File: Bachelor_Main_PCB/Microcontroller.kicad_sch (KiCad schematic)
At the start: 14 parts, among them J3 M20-9990245, J4 M20-9990245, J5 M20-9990245, U3 STM32H7A3ZITxQ, U4 USB3320C-EZK-TR, Y1 SG-210STF 24Mhz

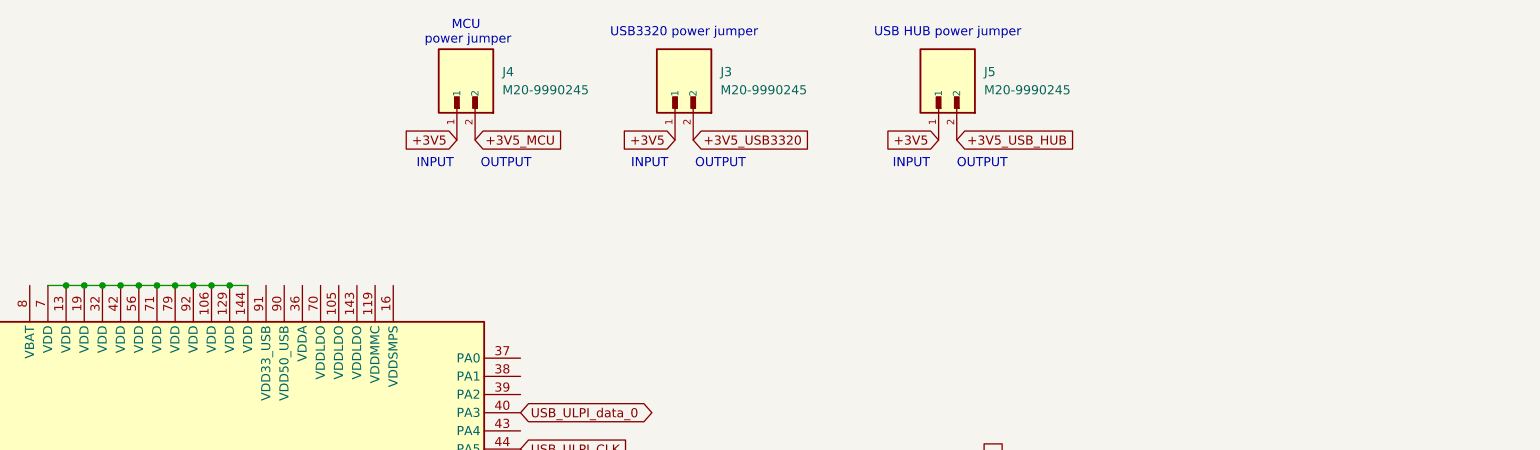
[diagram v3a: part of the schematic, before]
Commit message: Add 2,2uF inductor to MCU
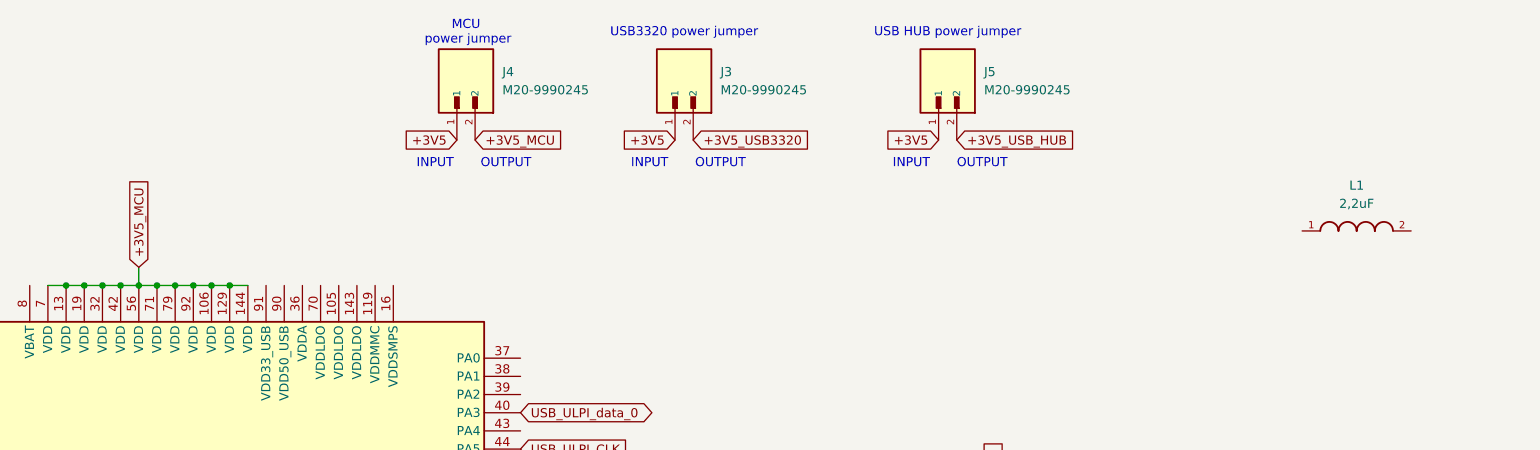
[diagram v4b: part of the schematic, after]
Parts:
- added L1: 2,2uF, DFE252012P-2R2M=P2:INDC2520X120N, symbol DFE252012P-2R2M_P2:DFE252012P-2R2M=P2
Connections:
- net +3V5_MCU: now also U3.106 (VDD), U3.129 (VDD), U3.13 (VDD), U3.144 (VDD), U3.19 (VDD), U3.32 (VDD), U3.42 (VDD), U3.56 (VDD), U3.7 (VDD), U3.71 (VDD), U3.79 (VDD), U3.92 (VDD)
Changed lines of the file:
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@@
 	(wire
 		(pts
+			(xy 90.17 53.34) (xy 90.17 55.88)
+		)
+		(stroke
+			(width 0)
+			(type default)
+		)
+	)
+	(wire
+		(pts
 			(xy 102.87 55.88) (xy 105.41 55.88)
 		)
@@
 		)
 	)
+	(global_label "+3V5_MCU"
+		(shape input)
+		(at 90.17 53.34 90)
+		(fields_autoplaced yes)
+		(effects
+			(font
+				(size 1.27 1.27)
+			)
+			(justify left)
+		)
+		(property "Intersheetrefs" "${INTERSHEET_REFS}"
+			(at 90.17 40.2553 90)
+			(effects
+				(font
+					(size 1.27 1.27)
+				)
+				(justify left)
+				(hide yes)
+			)
+		)
+	)
 	(global_label "USB_ULPI_data_1"
 		(shape bidirectional)
@@
 					(unit 1)
 				)
+			)
+		)
+	)
+	(symbol
+		(lib_id "DFE252012P-2R2M_P2:DFE252012P-2R2M=P2")
+		(at 260.35 48.26 0)
+		(unit 1)
+		(exclude_from_sim no)
+		(in_bom yes)
+		(on_board yes)
+		(dnp no)
+		(fields_autoplaced yes)
+		(property "Reference" "L1"
+			(at 260.35 41.91 0)
+			(effects
+				(font
+					(size 1.27 1.27)
+				)
+			)
+		)
+		(property "Value" "2,2uF"
+			(at 260.35 44.45 0)
+			(effects
+				(font
+					(size 1.27 1.27)
+				)
+			)
+		)
+		(property "Footprint" "DFE252012P-2R2M=P2:INDC2520X120N"
+			(at 260.35 48.26 0)
+			(effects
+				(font
+					(size 1.27 1.27)
+				)
+				(justify bottom)
+				(hide yes)
+			)
+		)
+		(property "Datasheet" ""
+			(at 260.35 48.26 0)
+			(effects
+				(font
+					(size 1.27 1.27)
+				)
+				(hide yes)
+			)
+		)
+		(property "Description" ""
+			(at 260.35 48.26 0)
+			(effects
+				(font
+					(size 1.27 1.27)
+				)
+				(hide yes)
+			)
+		)
+		(property "MF" "Murata Electronics"
+			(at 260.35 48.26 0)
+			(effects
+				(font
+					(size 1.27 1.27)
+				)
+				(justify bottom)
+				(hide yes)
+			)
+		)
+		(property "Description_1" "Inductor with Inductance: 2.2uH Tol. +/-20%, Package: 1008 (2520)"
+			(at 260.35 48.26 0)
+			(effects
+				(font
+					(size 1.27 1.27)
+				)
+				(justify bottom)
+				(hide yes)
+			)
+		)
+		(property "Package" "2520 Murata"
+			(at 260.35 48.26 0)
+			(effects
+				(font
+					(size 1.27 1.27)
+				)
+				(justify bottom)
+				(hide yes)
+			)
+		)
+		(property "Price" "None"
+			(at 260.35 48.26 0)
+			(effects
+				(font
+					(size 1.27 1.27)
+				)
+				(justify bottom)
+				(hide yes)
+			)
+		)
+		(property "SnapEDA_Link" "https://www.snapeda.com/parts/DFE252012P-2R2M=P2/Murata+Electronics+North+America/view-part/?ref=snap"
+			(at 260.35 48.26 0)
+			(effects
+				(font
+					(size 1.27 1.27)
+				)
+				(justify bottom)
+				(hide yes)
+			)
+		)
+		(property "MP" "DFE252012P-2R2M=P2"
+			(at 260.35 48.26 0)
+			(effects
+				(font
+					(size 1.27 1.27)
+				)
+				(justify bottom)
+				(hide yes)
+			)
+		)
+		(property "Availability" "In Stock"
+			(at 260.35 48.26 0)
+			(effects
+				(font
+					(size 1.27 1.27)
+				)
+				(justify bottom)
+				(hide yes)
+			)
+		)
+		(property "Check_prices" "https://www.snapeda.com/parts/DFE252012P-2R2M=P2/Murata+Electronics+North+America/view-part/?ref=eda"
+			(at 260.35 48.26 0)
+			(effects
+				(font
+					(size 1.27 1.27)
+				)
+				(justify bottom)
+				(hide yes)
+			)
+		)
+		(pin "2"
+		)
+		(pin "1"
+		)
+		(instances
+			(project ""
+				(path "/3544d663-329e-4884-b753-28436ca187e8/9cdc091d-5c59-45ee-8211-bdd0f330a333"
+					(reference "L1")
+					(unit 1)
+				)

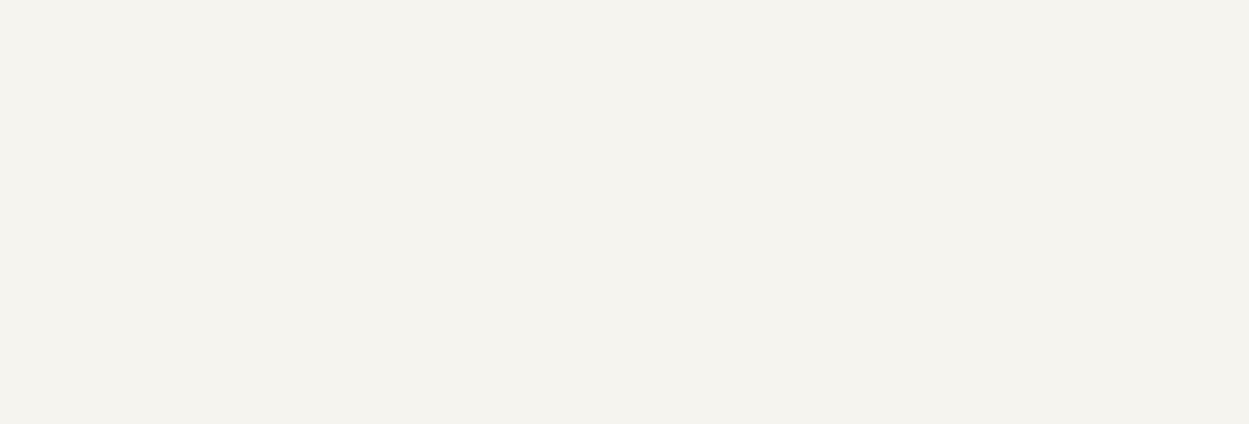
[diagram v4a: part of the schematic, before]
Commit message: Add MCU VDD caps
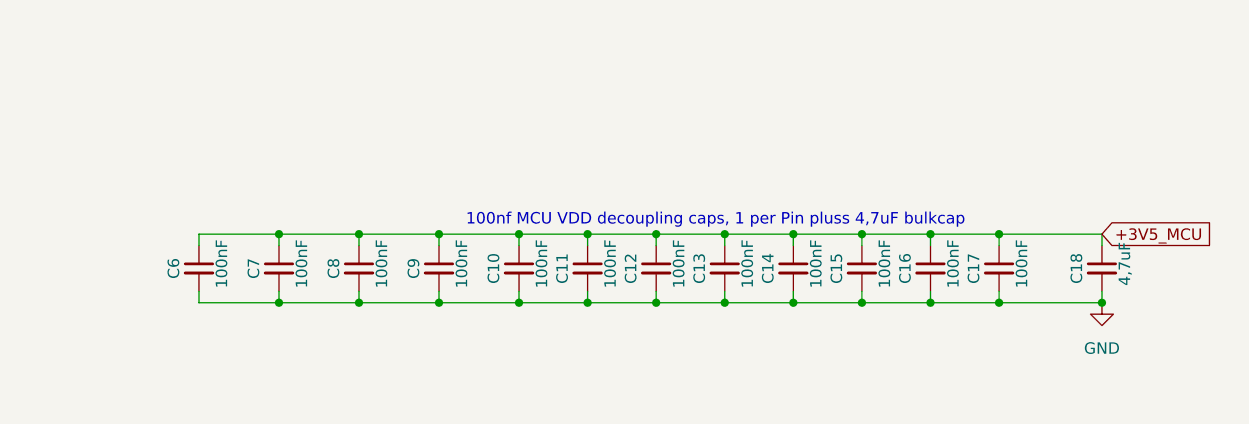
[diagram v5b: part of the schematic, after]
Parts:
- added C10, C11, C12, C13, C14, C15, C16, C17, C6, C7, C8, C9: 100nF, Capacitor_SMD:C_0603_1608Metric, symbol Device:C_Small
- added C18: 4,7uF, Capacitor_SMD:C_0603_1608Metric, symbol Device:C_Small
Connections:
- net +3V5_MCU: now also C10.1, C11.1, C12.1, C13.1, C14.1, C15.1, C16.1, C17.1, C18.1, C6.1, C7.1, C8.1, C9.1
- net GND: now also C10.2, C11.2, C12.2, C13.2, C14.2, C15.2, C16.2, C17.2, C18.2, C6.2, C7.2, C8.2, C9.2
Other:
- note added: "100nf MCU VDD decoupling caps, 1 per Pin pluss 4,7uF bulkcap"

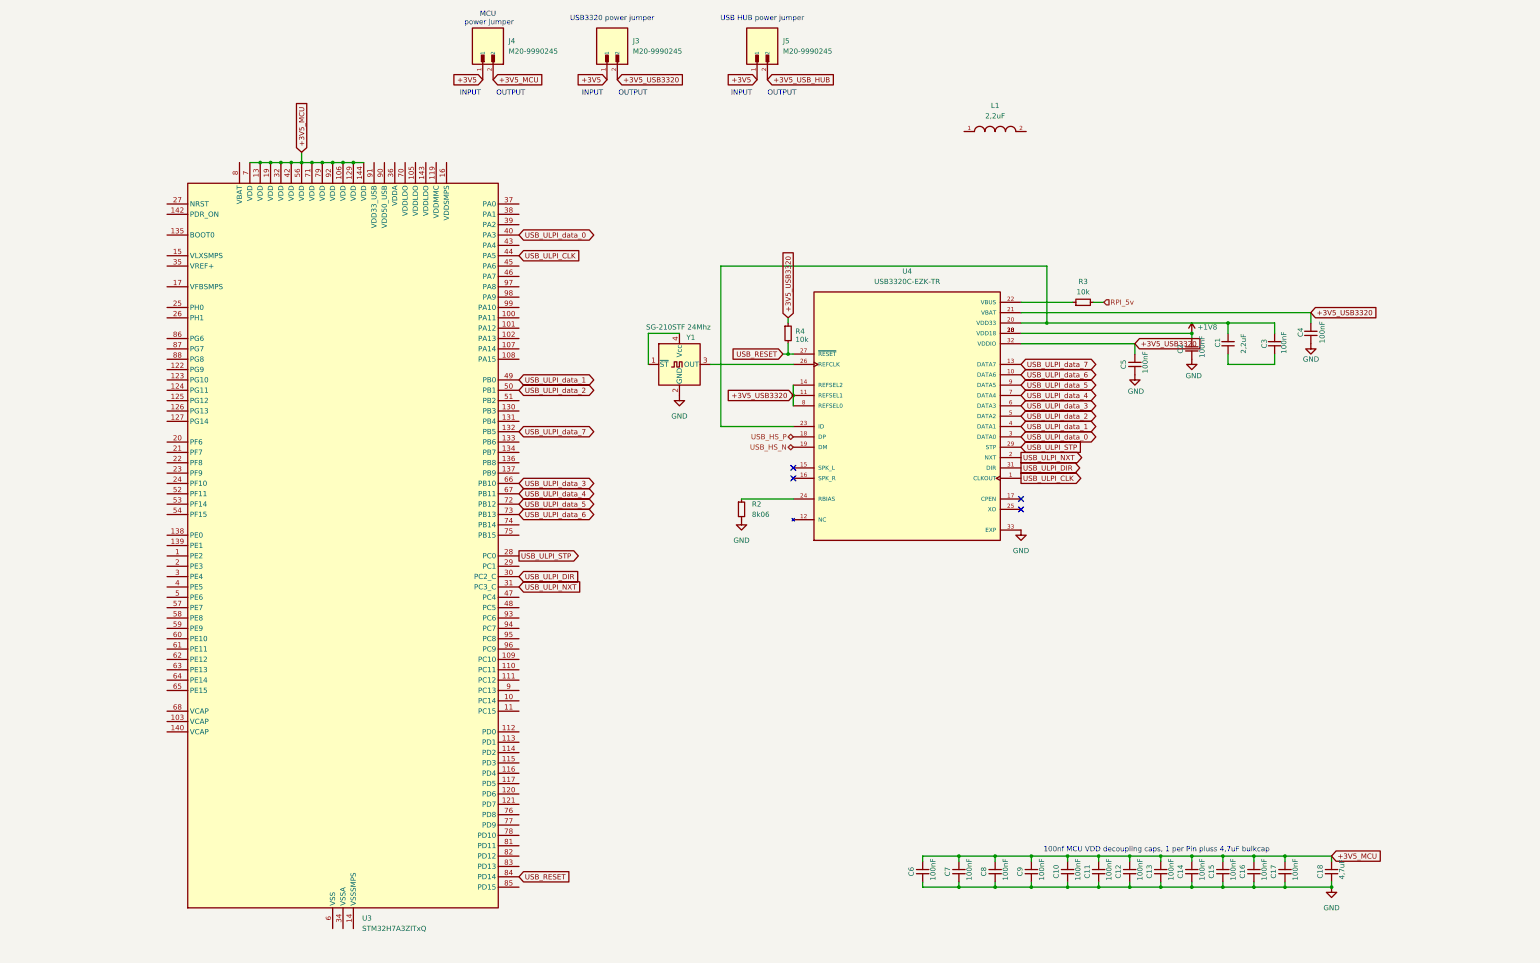
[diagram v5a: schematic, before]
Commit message: Add SMPS circuit
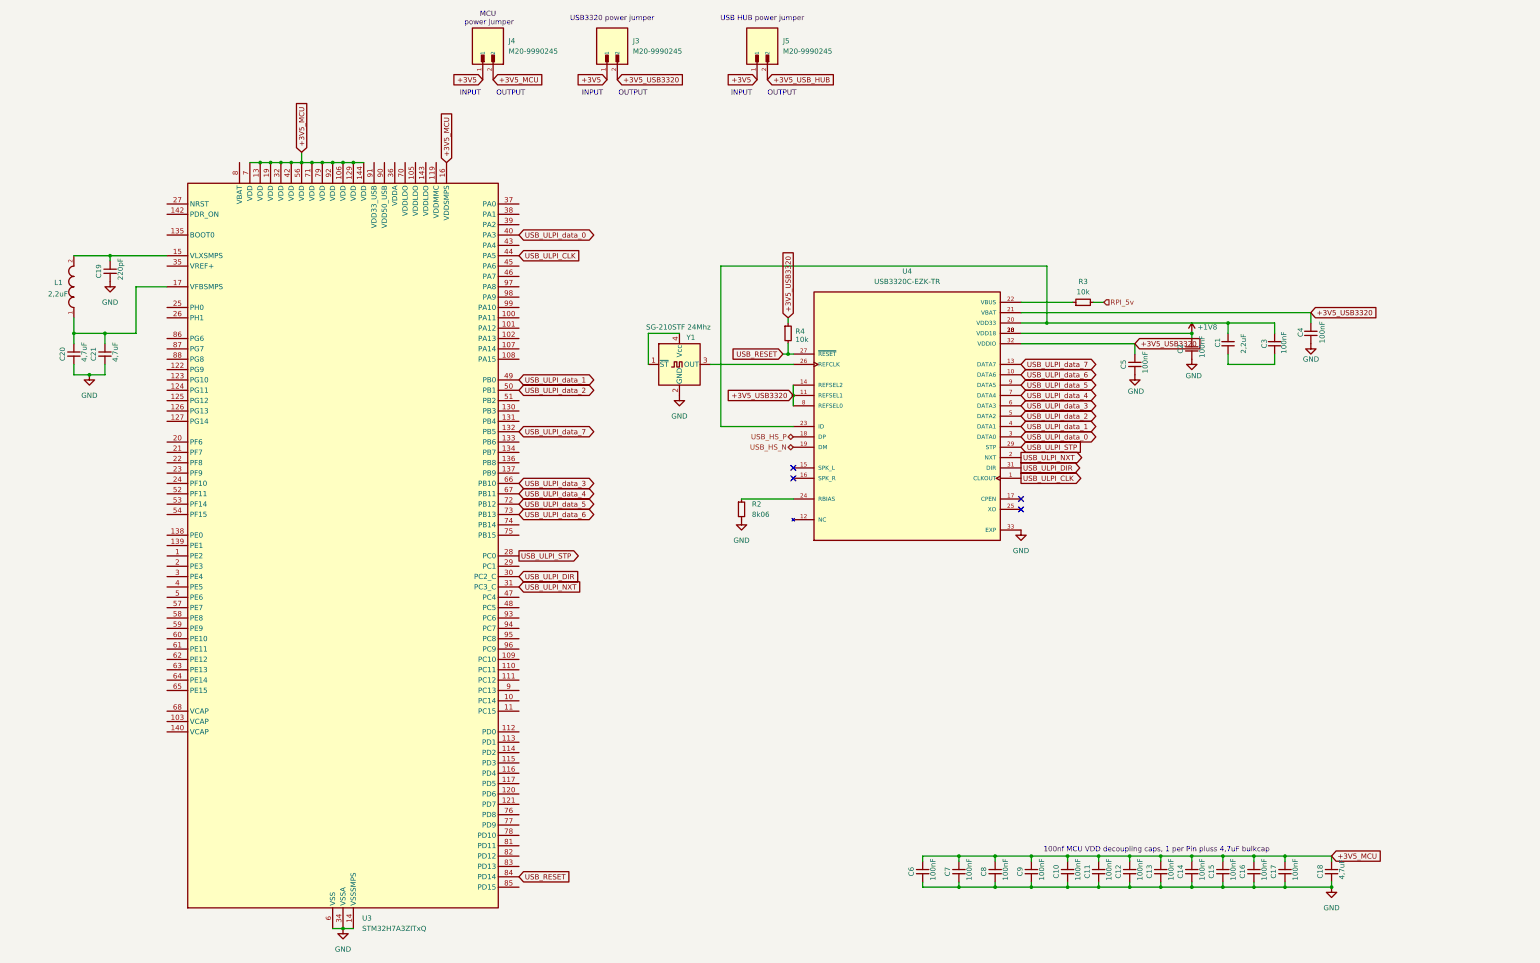
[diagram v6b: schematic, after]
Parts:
- added C19: 220pF, Capacitor_SMD:C_0603_1608Metric, symbol Device:C_Small
- added C20, C21: 4,7uF, Capacitor_SMD:C_0603_1608Metric, symbol Device:C_Small
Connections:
- net +3V5_MCU: now also U3.16 (VDDSMPS)
- net GND: now also U3.104 (VSS), U3.118 (VSS), U3.12 (VSS), U3.128 (VSS), U3.14 (VSSSMPS), U3.141 (VSS), U3.18 (VSS), U3.33 (VSS), U3.34 (VSSA), U3.41 (VSS), U3.55 (VSS), U3.6 (VSS), U3.69 (VSS), U3.80 (VSS), U3.89 (VSS), C19.2, C20.2, C21.2
- net at U3.15 (VLXSMPS): now also L1.2, C19.1
- net at U3.17 (VFBSMPS): now also L1.1, C20.1, C21.1
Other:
- moved on the sheet: L1

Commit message: VDDLDO add bypass caps
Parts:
- added C22, C23, C24: 100nF, Capacitor_SMD:C_0603_1608Metric, symbol Device:C_Small
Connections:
- net GND: now also C22.2, C23.2, C24.2
- net SMPS_out: now reaches U3.103 (VCAP)
- net SMPS_out: now also C20.1, C21.1, L1.1, U3.105 (VDDLDO), U3.140 (VCAP), U3.143 (VDDLDO), U3.17 (VFBSMPS), U3.68 (VCAP), U3.70 (VDDLDO), C22.1, C23.1, C24.1
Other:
- note added: "VDDLDO bypass caps, 1 per Pin"
